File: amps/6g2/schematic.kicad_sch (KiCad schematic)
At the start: 50 parts, among them T1 125P1A, T2 125A10B

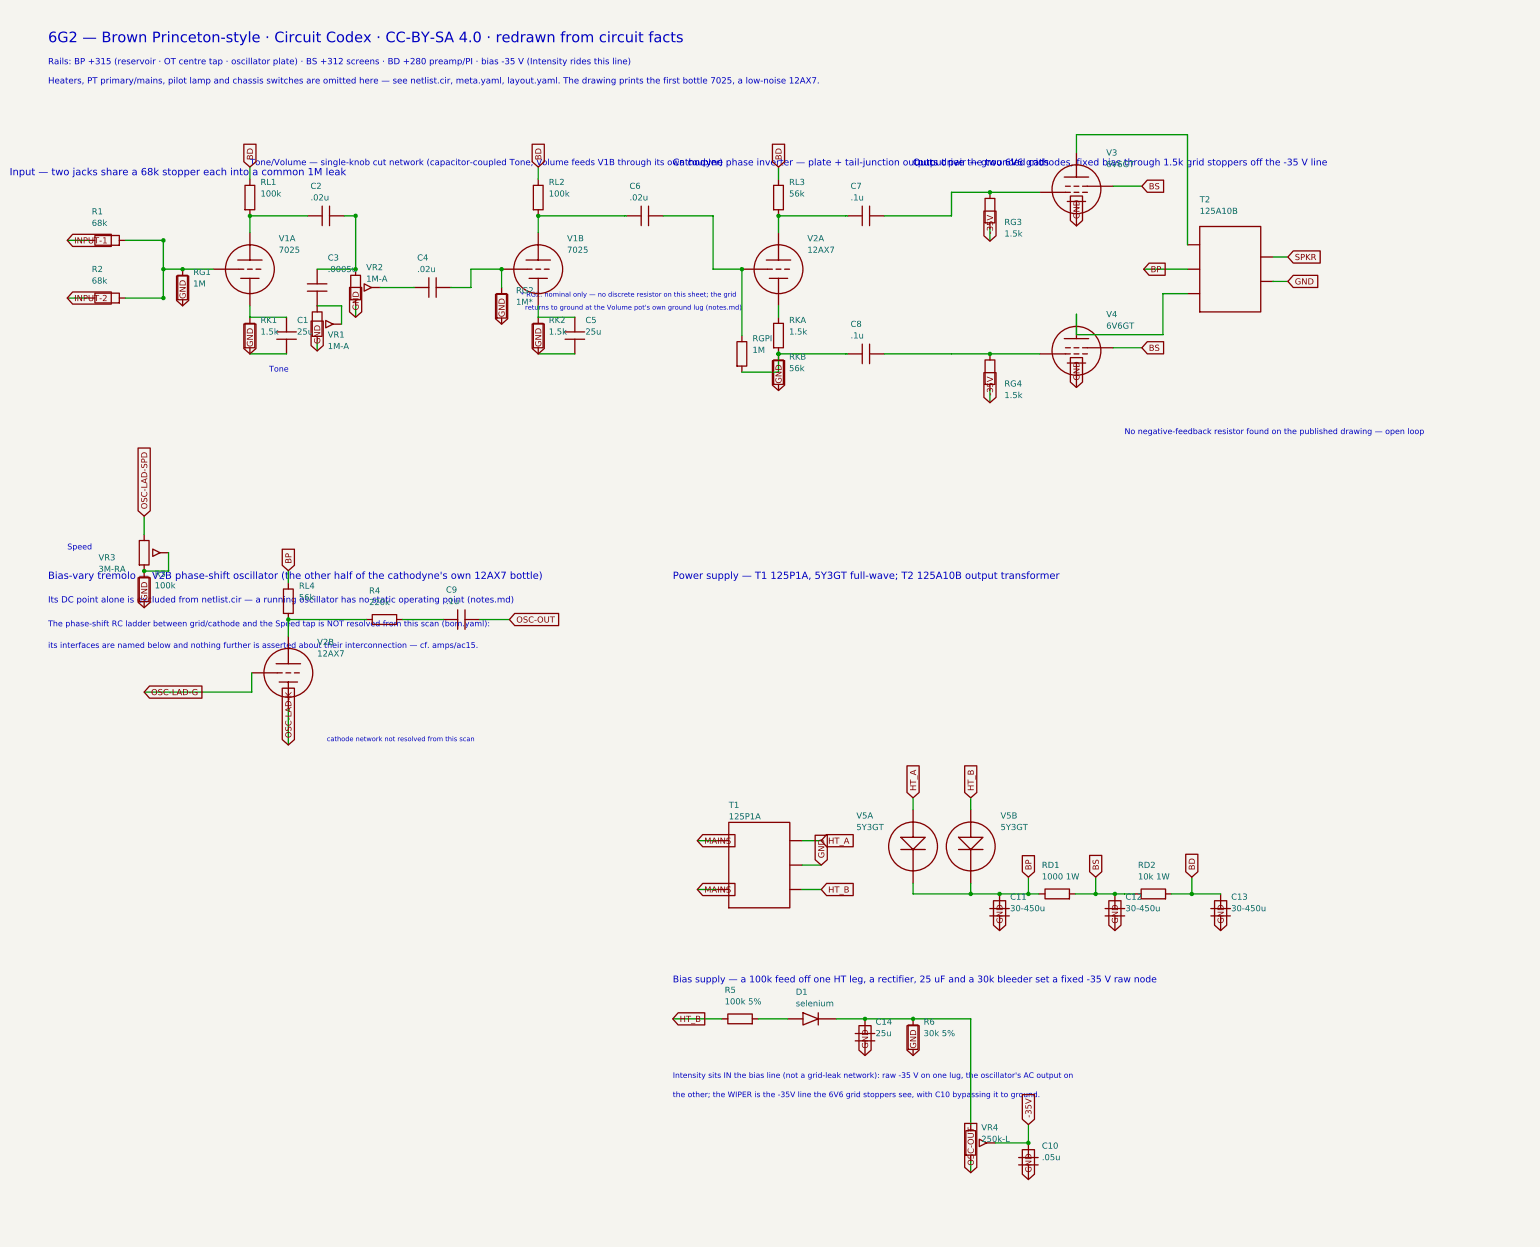
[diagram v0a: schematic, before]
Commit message: Fix: one lettering convention per surface, engine-enforced; legend inside the viewBox
WS3 — layout pipeline + cross-surface value-consistency engine.

## One convention per surface (docs/lettering-conventions.md, new)

The same part stated its value in several notations at once. 5E3 C6 and 5D3 C6
rendered "5n" on the schematic, "0.005 µF · 600 V" in the parts list and
"0.005 µF" on the board. 5F6-A RD1 printed "4,700 Ω" beside neighbours printing
"15 kΩ". check_value_consistency proves the surfaces name the same QUANTITY; it
cannot see that they name it three ways. So each surface now has exactly one
convention and every one of them is gated:

* house units in bom.yaml/prose — engineering prefix with the mantissa 1…999,
  pF below 1000 pF and µF at and above it, no comma-grouped thousands. 19 values
  normalised (5E6-A, 5F6-A, 5F10, 6161, 6G2, 6G5, 6G6-B).
* schematic drafting shorthand — the unit letter is the SI prefix of the house
  unit, in the amp's declared idiom (meta.yaml conventions.notation: us|uk).
  British RKM/nanofarad practice on the Hiwatt and the 2204 is DECLARED, not
  normalised away; it is what those source drawings letter. Secondary ratings
  are space-separated fields with their own unit ("20u 600V"), never the era's
  dashed shorthand and never the house middot. 30 symbol values corrected across
  ten draw scripts.
* era sheet lettering — generated only, by era_pair(); documented cases and a
  corpus round-trip sweep in test_era_values.py, now 57 cases.

## Era-lettering fall-throughs closed

A value era_pair() refuses came back as the house string, and a house string can
be a whole sentence. Fixed at the source rather than per case:

* body_value() — a parenthetical GLOSS is never lettered on a component body.
  "selenium (silicon diode in modern builds)" was lettered in full on the 5E4-A
  and ran off the left edge of the page.
* twin cans letter as the era sheets did: 25 µF + 25 µF -> "25/25MFD".
* a repeat count is not a rating: "(×2)" com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
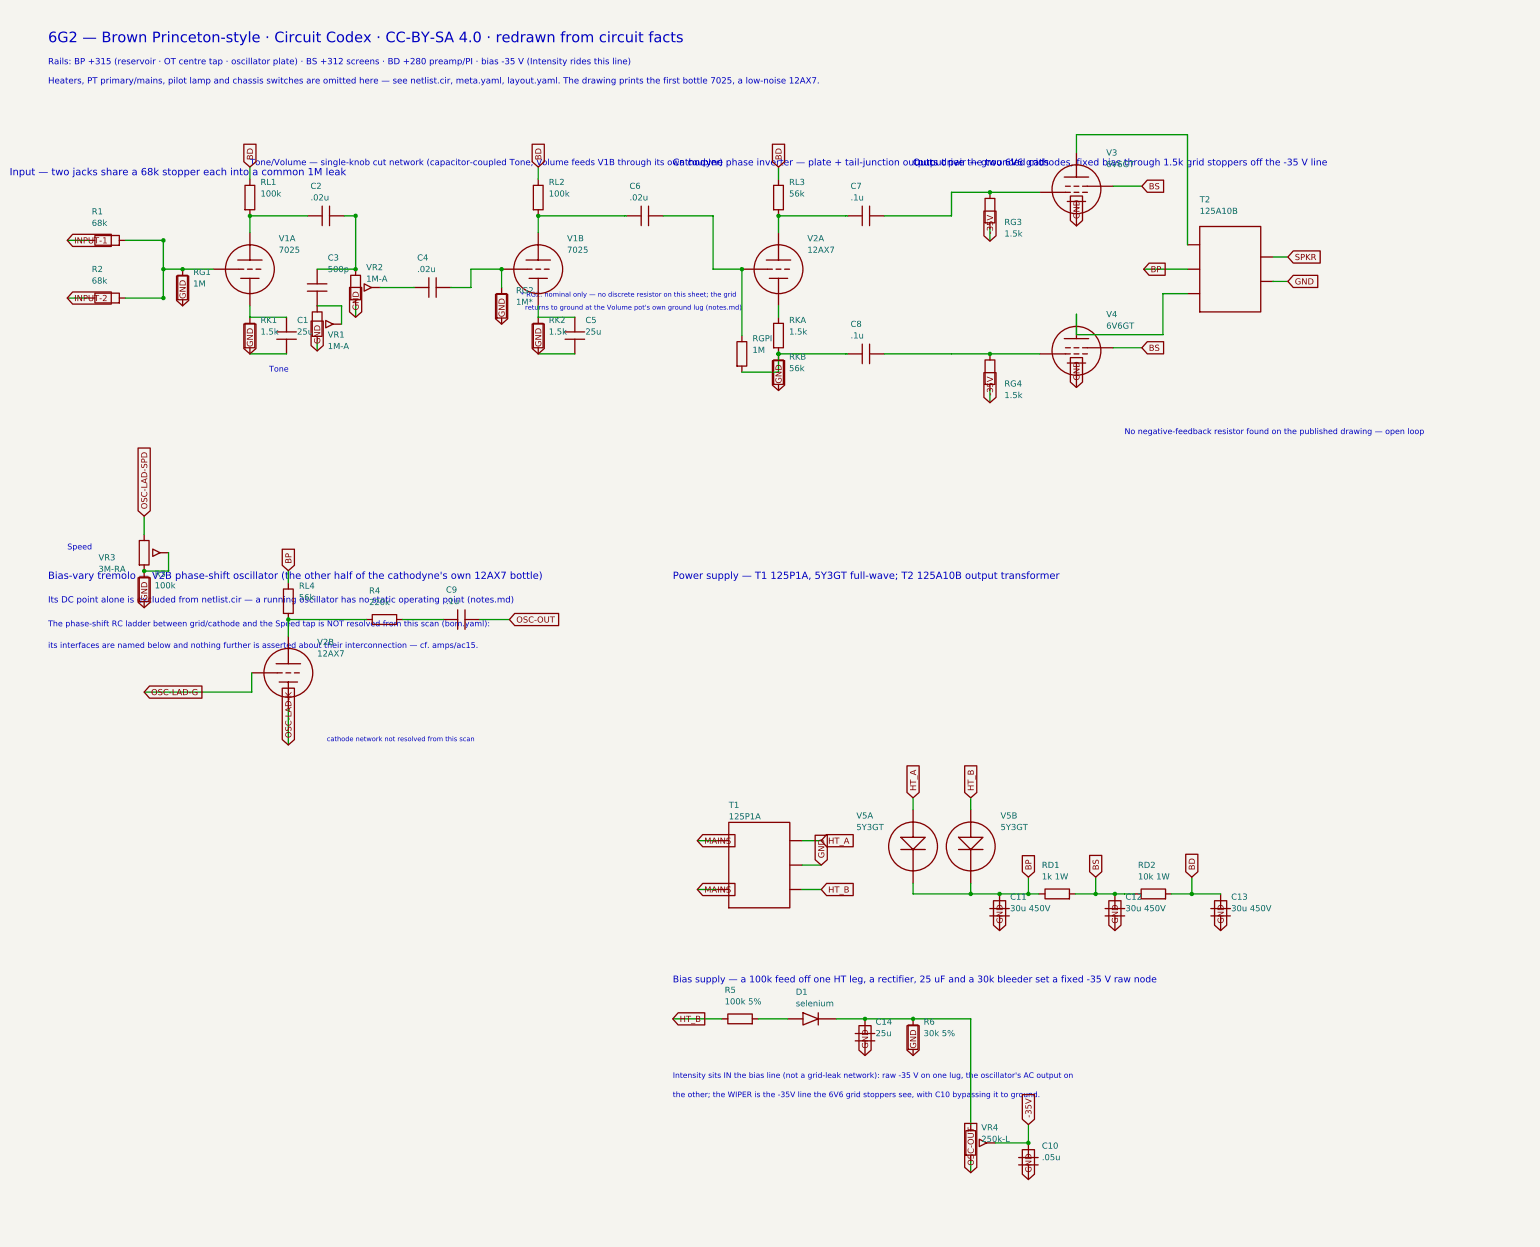
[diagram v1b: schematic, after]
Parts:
- C11, C12, C13: value 30-450u -> 30u 450V
- C3: value .0005u -> 500p
- RD1: value 1000 1W -> 1k 1W
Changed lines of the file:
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@@
     (in_bom yes) (on_board yes)
     (property "Reference" "C3" (at 78.2 63.61 0) (effects (font (size 1.27 1.27)) (justify left)))
-    (property "Value" ".0005u" (at 78.2 66.01 0) (effects (font (size 1.27 1.27)) (justify left))))
+    (property "Value" "500p" (at 78.2 66.01 0) (effects (font (size 1.27 1.27)) (justify left))))
   (symbol (lib_id "cx:POT") (at 76 77.43 0) (unit 1)
     (in_bom yes) (on_board yes)
@@
     (in_bom yes) (on_board yes)
     (property "Reference" "C11" (at 220.2 196.61 0) (effects (font (size 1.27 1.27)) (justify left)))
-    (property "Value" "30-450u" (at 220.2 199.01 0) (effects (font (size 1.27 1.27)) (justify left))))
+    (property "Value" "30u 450V" (at 220.2 199.01 0) (effects (font (size 1.27 1.27)) (justify left))))
   (global_label "GND" (shape input) (at 218 203.62 270)
     (effects (font (size 1.27 1.27)) (justify left)))
@@
     (in_bom yes) (on_board yes)
     (property "Reference" "RD1" (at 226.8 190 270) (effects (font (size 1.27 1.27)) (justify left)))
-    (property "Value" "1000 1W" (at 226.8 192.4 270) (effects (font (size 1.27 1.27)) (justify left))))
+    (property "Value" "1k 1W" (at 226.8 192.4 270) (effects (font (size 1.27 1.27)) (justify left))))
   (wire (pts (xy 224 196) (xy 226.19 196))
     (stroke (width 0) (type default)))
@@
     (in_bom yes) (on_board yes)
     (property "Reference" "C12" (at 244.2 196.61 0) (effects (font (size 1.27 1.27)) (justify left)))
-    (property "Value" "30-450u" (at 244.2 199.01 0) (effects (font (size 1.27 1.27)) (justify left))))
+    (property "Value" "30u 450V" (at 244.2 199.01 0) (effects (font (size 1.27 1.27)) (justify left))))
   (global_label "GND" (shape input) (at 242 203.62 270)
     (effects (font (size 1.27 1.27)) (justify left)))
@@
     (in_bom yes) (on_board yes)
     (property "Reference" "C13" (at 266.2 196.61 0) (effects (font (size 1.27 1.27)) (justify left)))
-    (property "Value" "30-450u" (at 266.2 199.01 0) (effects (font (size 1.27 1.27)) (justify left))))
+    (property "Value" "30u 450V" (at 266.2 199.01 0) (effects (font (size 1.27 1.27)) (justify left))))
   (global_label "GND" (shape input) (at 264 203.62 270)
     (effects (font (size 1.27 1.27)) (justify left)))

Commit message: Update: regenerate every drawing the four merged units changed
The four parallel units all rewrote generators, so their committed artifacts
were each generated against only their own third of the merged pipeline. Every
schematic, both layout styles, the social cards and the manifest are rebuilt
here from the merged sources, so what ships is what the merged generators draw.

One integration fault the rebuild exposed, invisible to any single unit:

- 5E5-A: the note explaining that the Presence wiper and the 100k feedback
  resistor land on V3A's GRID (not its cathode, as on the 5F4) was added as a
  hand-placed `s.text()` at a coordinate chosen before the sheet gained a
  reserved notes band. Merged, it printed through the -32V bias label. Moved to
  `note()`, which wraps prose into that band — the exact failure mode the band
  was built to end.

Three conflicts resolved against docs/lettering-conventions.md rather than by
picking a side, since two units had corrected the same lines for different
reasons:

- 5E5-A tone/feedback caps take the corrected designators (C7, C8, C9, RNF —
  `C_tr1`/`C_NFB` were generator identifiers that had leaked onto a published
  board) with the house-derived lettering (`.01u 400V`, `500p`, `.1u 200V`).
  Dropping the working voltage or writing `.0005u` would have lost a rating the
  source prints and re-broken the pF/µF decade rule.
- 5D3 C6 and 6G6-B's three cathode resistors take the SI-prefix form the
  convention binds (`.005u`, `2.7k`, `1.5k`), keeping the ground-flag direction
  fix and the removal of the second `gnd()` that shorted each cathode it biased.
- 5F6-A's bias supply keeps both 8 µF cans drawn — the second was previously a
  parenthetical claiming one of two was shown — at the coordinates that clear
  the title-block strip.

All gates green, including check_value_consistency at zero disagreements.

🤖 Generated with [Claude Code](https://claude.com/claude-code)

Co-Authored-By: Claude Fable 5 <noreply@anthropic.com>
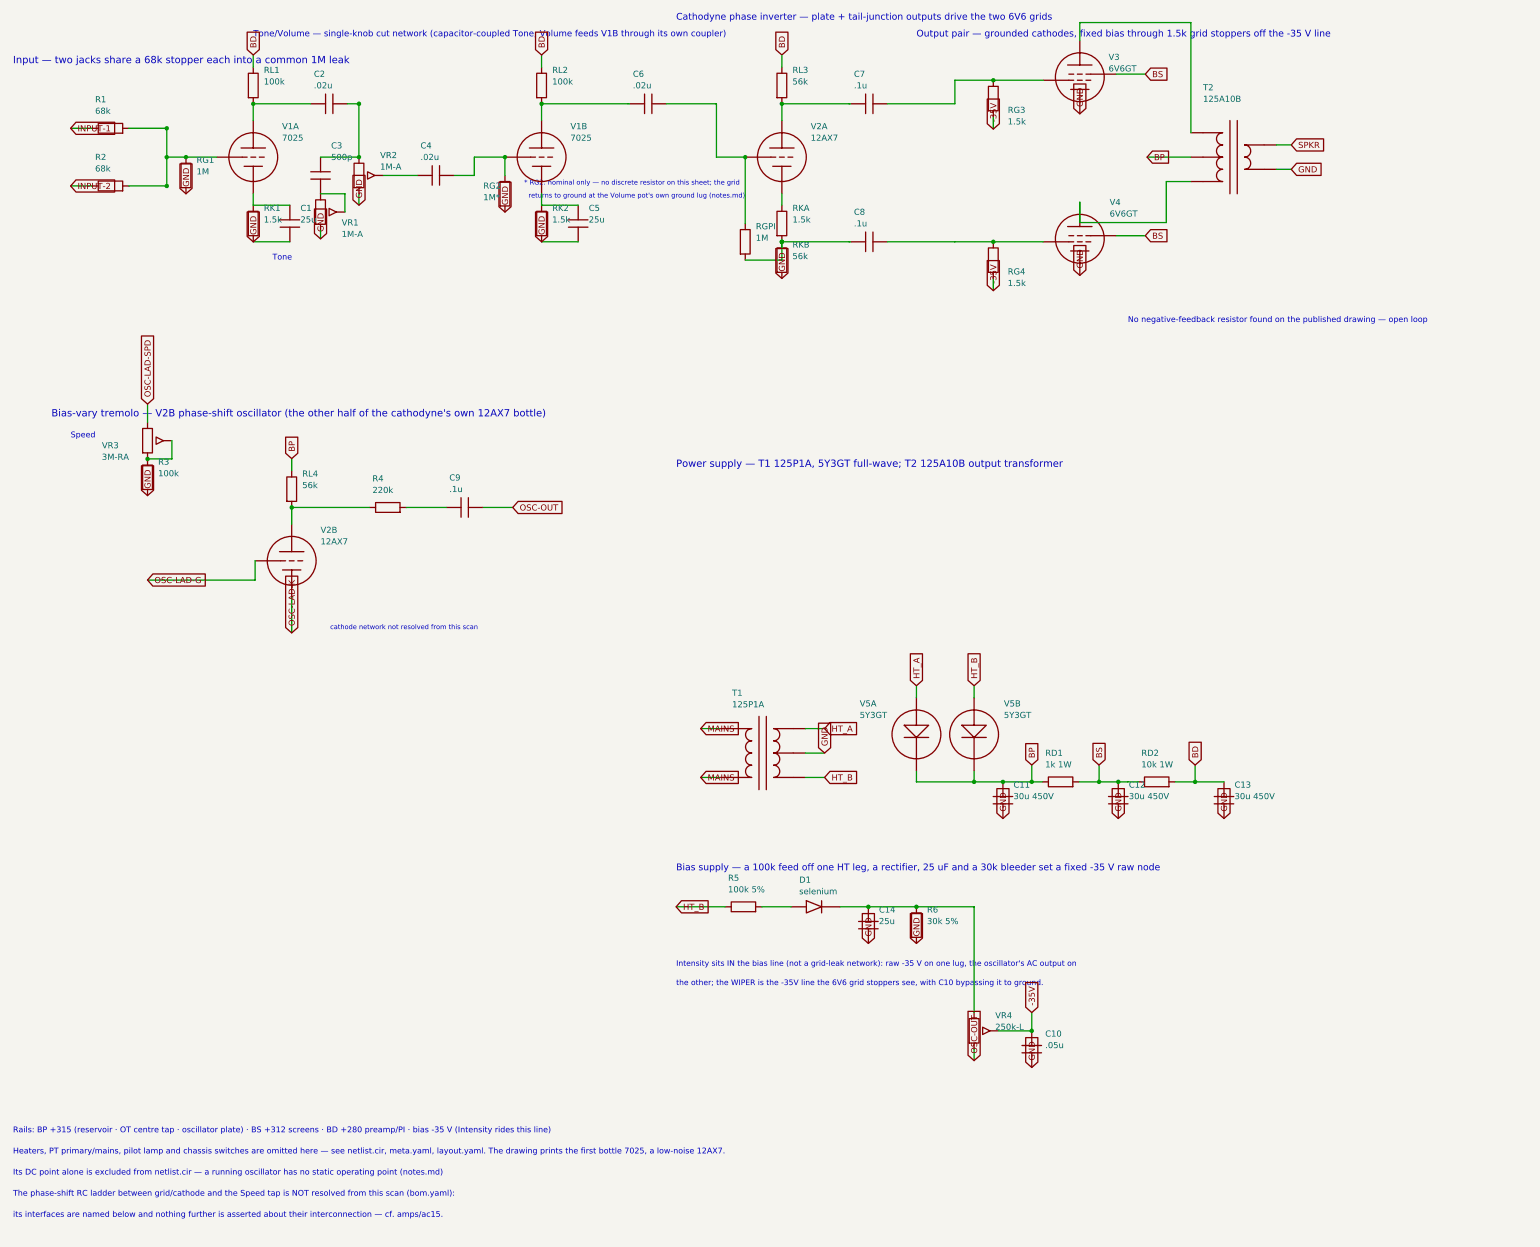
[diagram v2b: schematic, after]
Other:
- note removed: "6G2 — Brown Princeton-style · Circuit Codex · CC-BY-SA 4.0 · redrawn from circuit facts"
- company: (none) -> Circuit Codex
- title: (none) -> 6G2 — Brown Princeton-style
